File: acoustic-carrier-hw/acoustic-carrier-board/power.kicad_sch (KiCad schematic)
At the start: 71 parts, among them J2 Conn_02x08_Odd_Even, Q2 AO3401A, U17 TPS2121RUX, U19 TLV62569DBV, U21 TLV62569DBV, U24 TLV62569DBV, U25 TLV62569DBV, U26 OPA376xxDBV

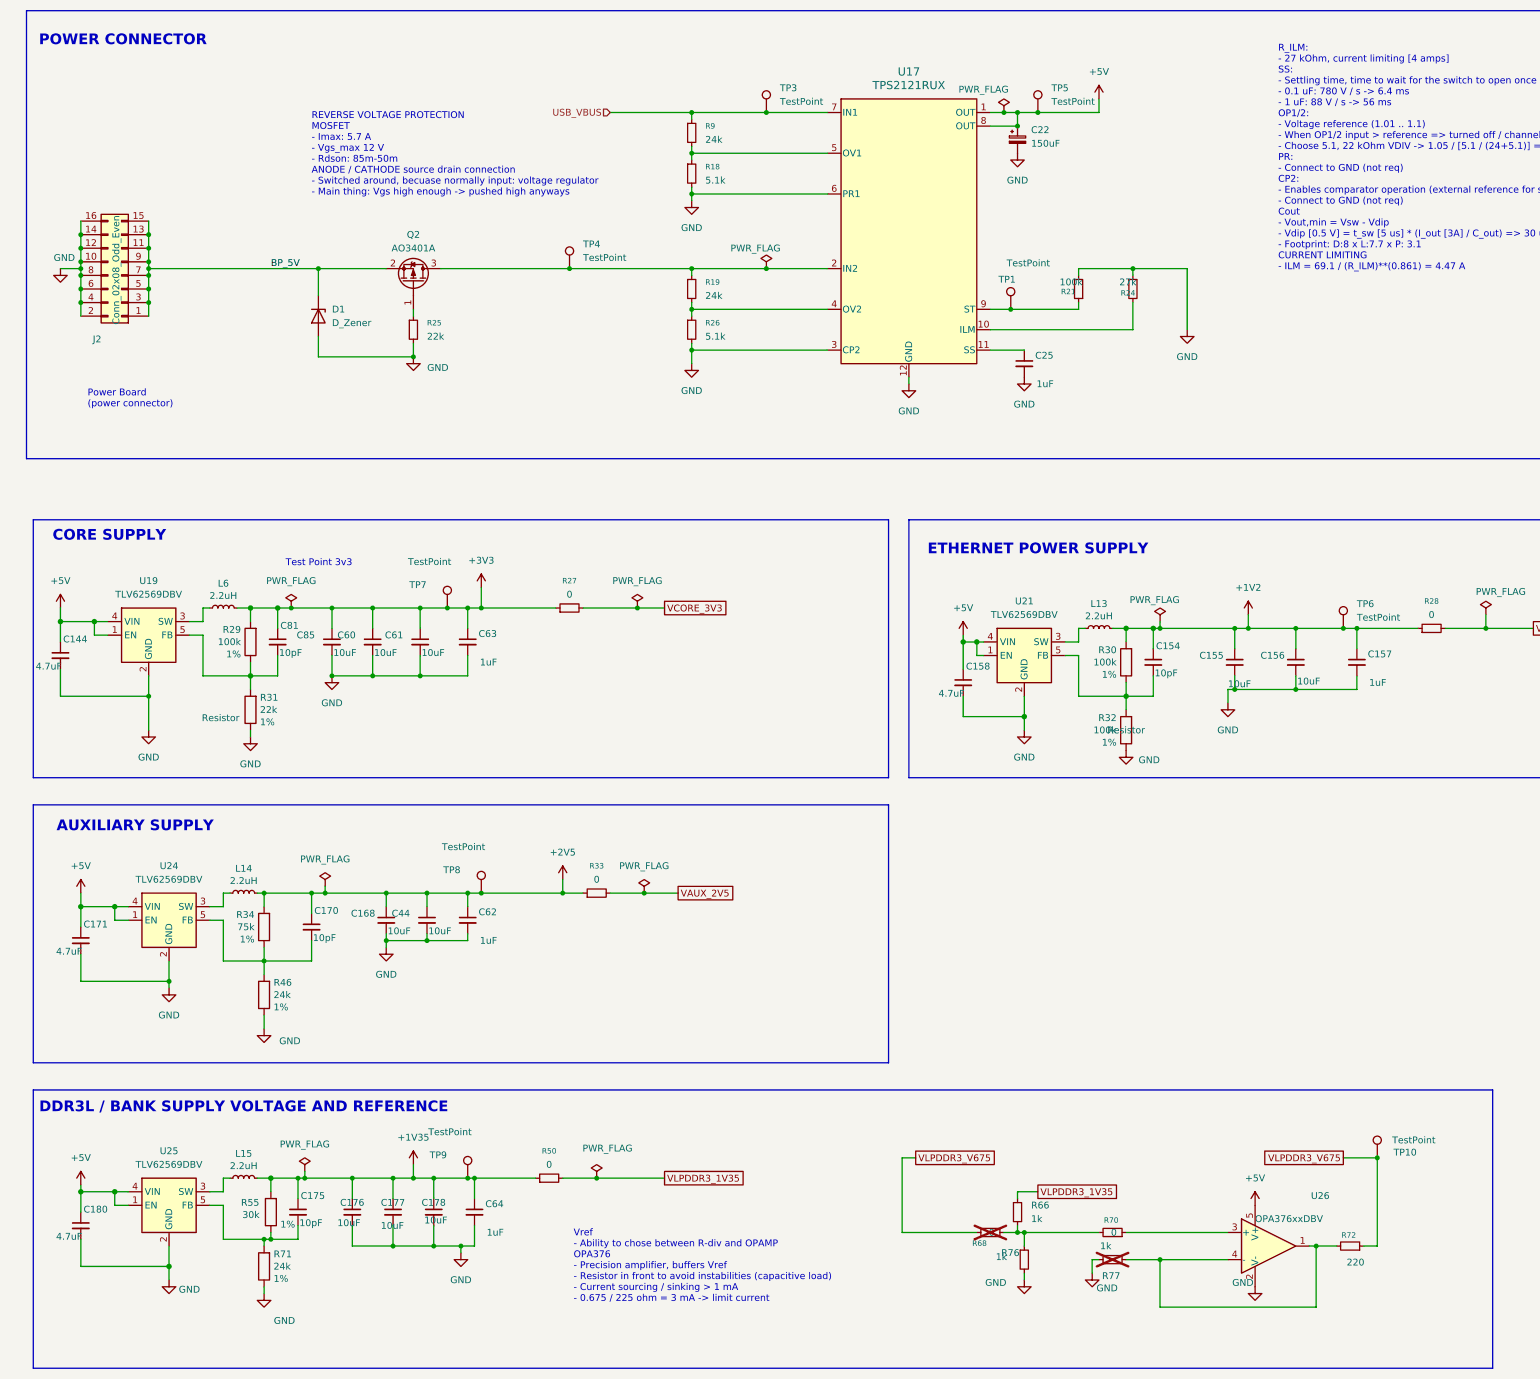
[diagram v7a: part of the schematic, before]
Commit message: [carrier] Finished rough layout, p (put together according to component category
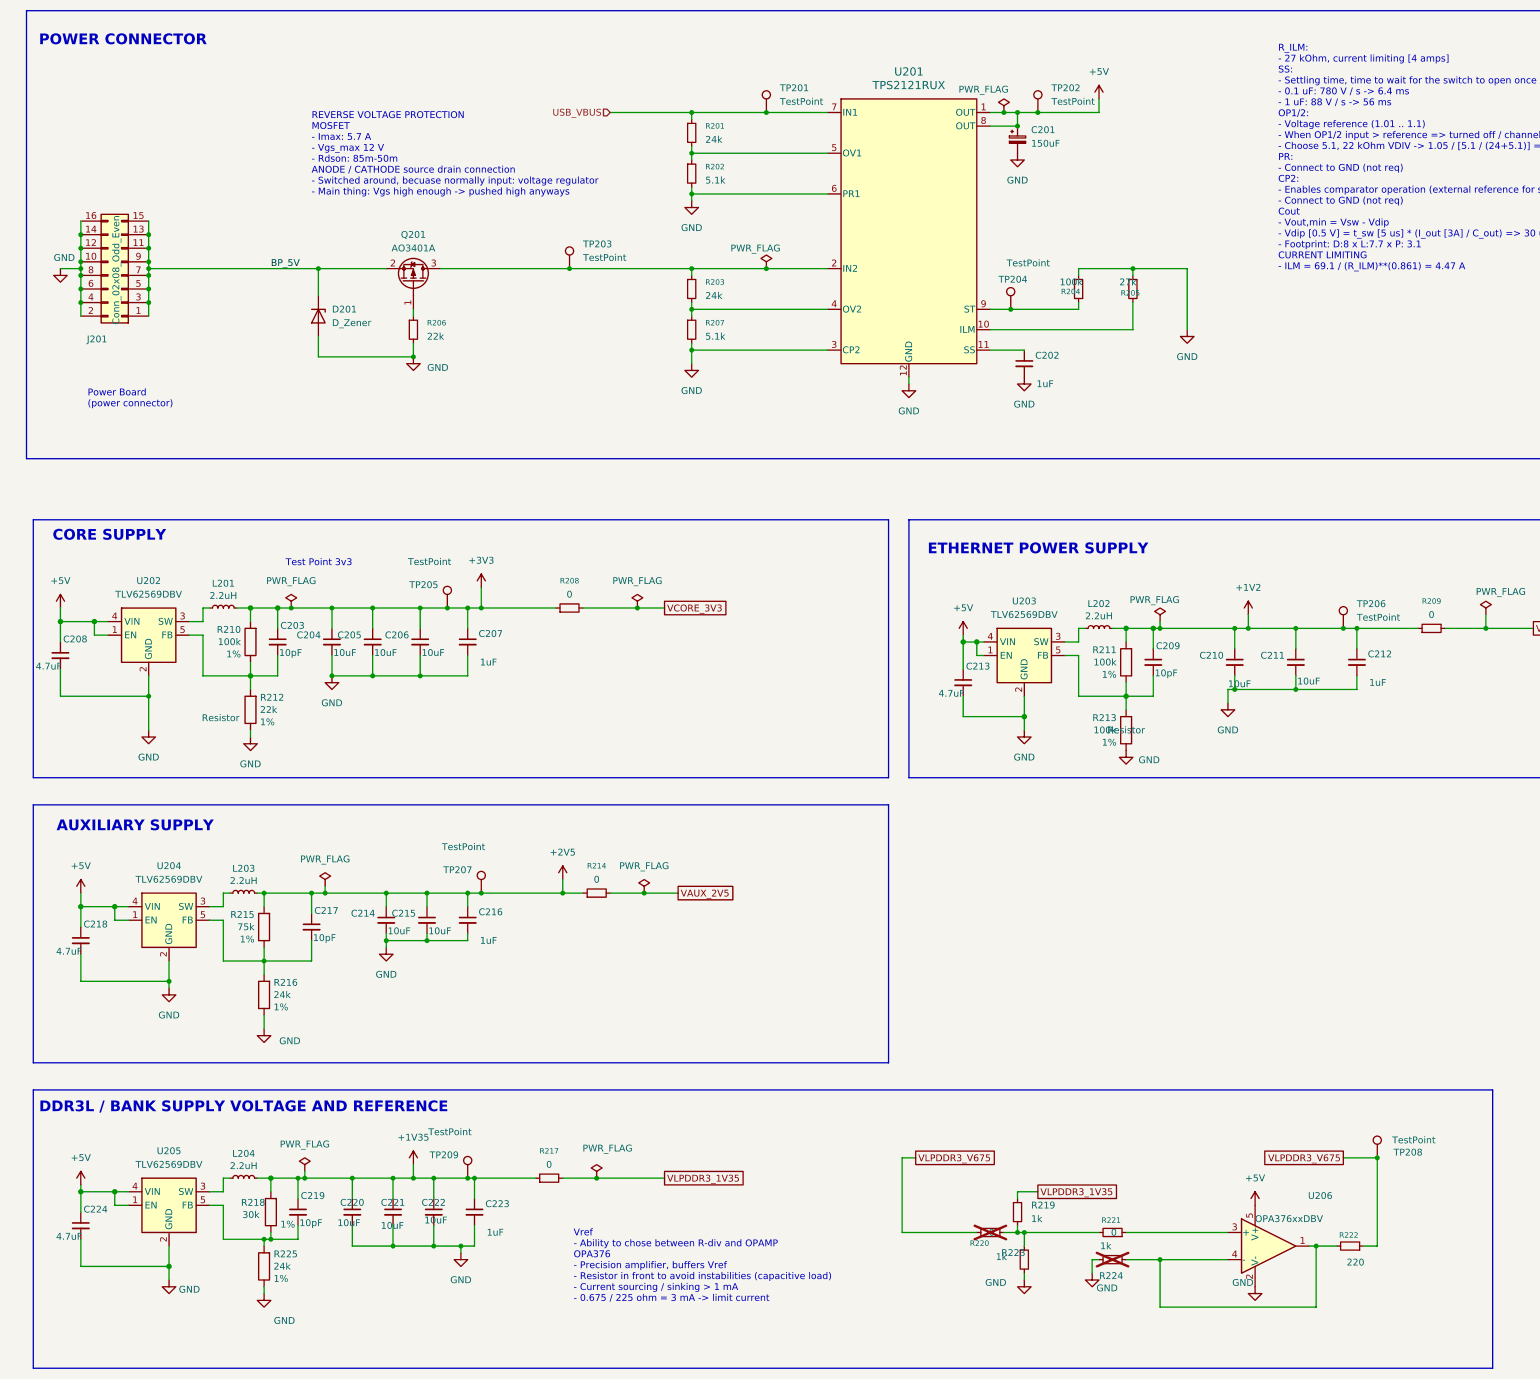
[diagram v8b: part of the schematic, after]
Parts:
- renumbered C22 to C201, C25 to C202, C81 to C203, C85 to C204, C60 to C205, C61 to C206, C63 to C207, C144 to C208, C154 to C209, C155 to C210, C156 to C211, C157 to C212, C158 to C213, C168 to C214, C44 to C215, C62 to C216, C170 to C217, C171 to C218, C175 to C219, C176 to C220, C177 to C221, C178 to C222, C64 to C223, C180 to C224, D1 to D201, J2 to J201, L6 to L201, L13 to L202, L14 to L203, L15 to L204, Q2 to Q201, R9 to R201, R18 to R202, R19 to R203, R21 to R204, R24 to R205, R25 to R206, R26 to R207, R27 to R208, R28 to R209, R29 to R210, R30 to R211, R31 to R212, R32 to R213, R33 to R214, R34 to R215, R46 to R216, R50 to R217, R55 to R218, R66 to R219, R68 to R220, R70 to R221, R72 to R222, R76 to R223, R77 to R224, R71 to R225, TP3 to TP201, TP5 to TP202, TP4 to TP203, TP1 to TP204, TP7 to TP205, TP6 to TP206, TP8 to TP207, TP10 to TP208, TP9 to TP209, U17 to U201, U19 to U202, U21 to U203, U24 to U204, U25 to U205, U26 to U206
